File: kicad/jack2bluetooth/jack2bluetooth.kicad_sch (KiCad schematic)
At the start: 153 parts, among them IC1 TLV320AIC3101IRHBR, IC2 BQ25619RTWR, IC3 MCP23008T-E_SO, IC4 TPS62A01PDDCR, IC5 TPS62A01PDDCR, IC7 ESP32-WROVER-E-N16R8, J1 SJ3-35063A, J10 Conn_01x03_Pin, J2 USB_C_Receptacle, J3 Conn_01x03_Pin, J4 SJ1-2503A, J5 Conn_01x03_Pin, J6 Conn_01x04_Pin, J7 Conn_01x02_Pin, J8 Conn_01x02_Pin, J9 Conn_01x08_Pin, Q1 DMP3099L-13, Q2 BC846, Q3 BC846, SW1 SW_Push, SW2 SW_Push, SW3 SW_Push, SW4 SW_Push, SW5 SW_SPDT, SW6 SW_Push, SW7 SW_SPDT

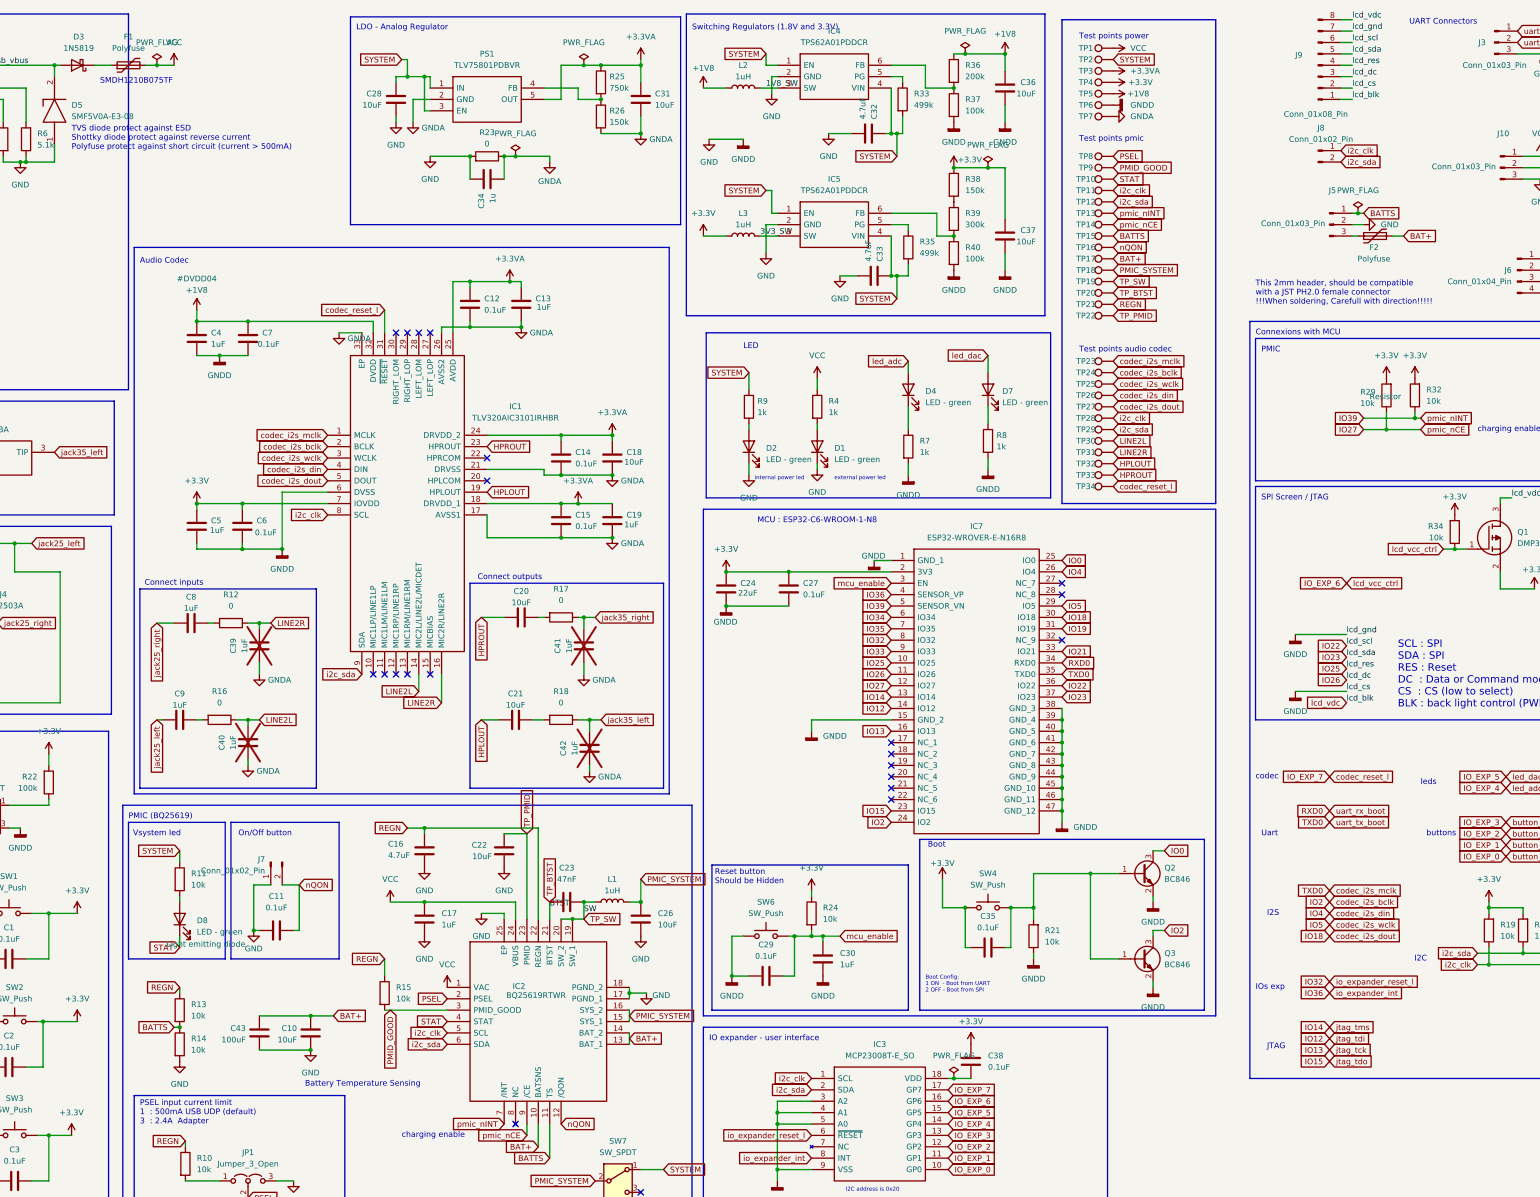
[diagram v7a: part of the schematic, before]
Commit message: feat: route power
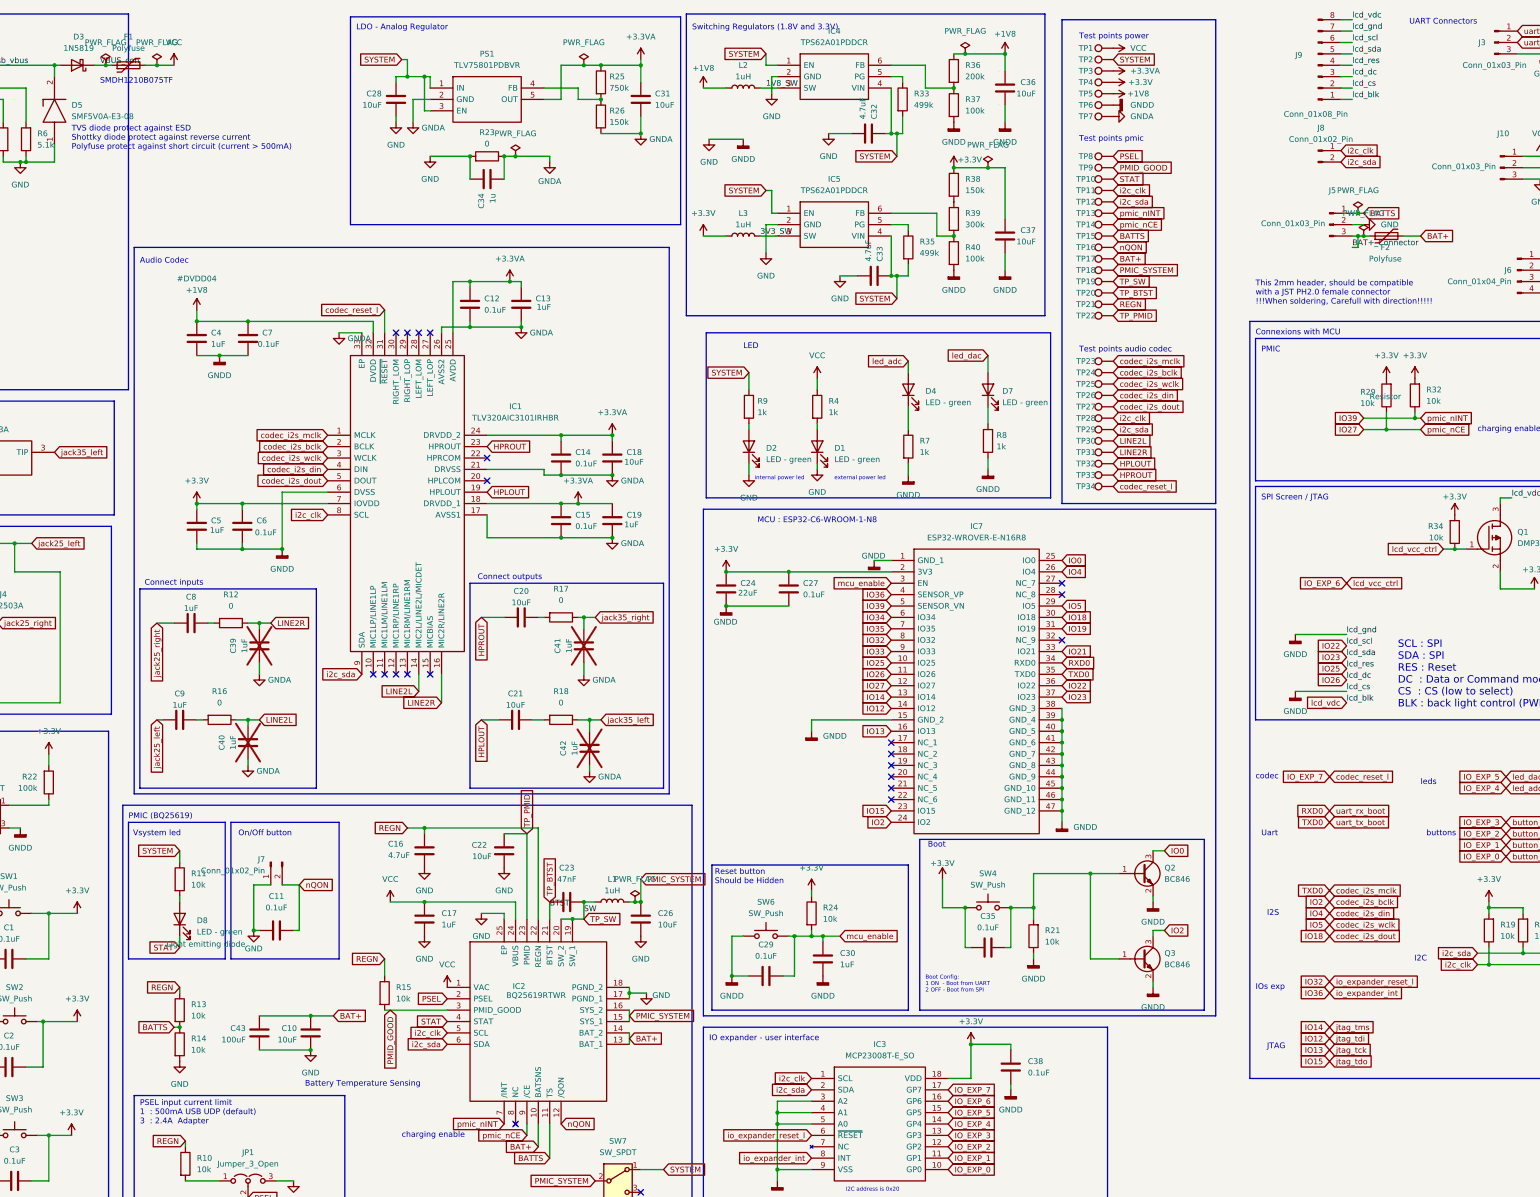
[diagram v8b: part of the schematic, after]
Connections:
- net +3.3V: now also IC3.18 (VDD)
- net GND: now also C38.2
- net VBUS_con: now reaches D3.1 (K), F1.1
- net BAT+_Connector: now reaches F2.1, J5.3 (Pin_3)
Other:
- moved on the sheet: C38, F2
